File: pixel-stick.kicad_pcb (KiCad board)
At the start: 2 copper layers, 16.5 x 37.1 mm, 15 parts, among them J2 WS28**, U1 AZ1117-3.3, U2 ESP-01v090, U3 SN74LVC1T45DBV, U4 RT9361A

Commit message: address DRC errors
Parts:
- moved R3 5.94 mm to (55.5, 65.0)
- moved NT1 2.17 mm to (52.8, 83.6)
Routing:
- net Net-(R3-Pad1): track 4.21 -> 7.34 mm
- net +3V3: track 19.9 -> 16.9 mm
- net /GPIO0: track 27.3 -> 25.4 mm
- net /CLOCK: track 1.53 -> 3.17 mm
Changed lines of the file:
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@@
   )
   (setup
-    (last_trace_width 0.5)
+    (last_trace_width 0.25)
     (user_trace_width 0.5)
     (user_trace_width 1)
@@
   )
   (module NetTie:NetTie-2_SMD_Pad0.5mm (layer B.Cu)
-    (at 52.832 85.725 270)
+    (at 52.832 83.558 270)
     (descr "Net tie, 2 pin, 0.5mm square SMD pads")
     (tags "net tie")
@@
   )
   (module Resistor_SMD:R_0805_2012Metric (layer F.Cu)
-    (at 49.7055 66.548)
+    (at 55.4505 65.024)
     (descr "Resistor SMD 0805 (2012 Metric), square (rectangular) end terminal, IPC_7351 nominal, (Body size source: https://docs.google.com/spreadsheets/d/1BsfQQcO9C6DZCsRaXUlFlo91Tg2WpOkGARC1WS5S8t0/edit?usp=sharing), generated with kicad-footprint-generator")
     (tags resistor)
@@
   (segment (start 46.299999 70.393999) (end 48.668999 70.393999) (width 0.5) (layer F.Cu) (net 2))
   (segment (start 46.035 71.374) (end 46.035 70.658998) (width 0.5) (layer F.Cu) (net 2))
-  (segment (start 50.643 66.548) (end 50.643 67.348) (width 0.5) (layer F.Cu) (net 2))
-  (segment (start 50.643 64.775) (end 50.968 64.45) (width 0.5) (layer F.Cu) (net 2))
-  (segment (start 50.643 66.548) (end 50.643 64.775) (width 0.5) (layer F.Cu) (net 2))
   (segment (start 52.324 54.864) (end 55.946202 54.864) (width 1) (layer F.Cu) (net 2))
   (segment (start 52.04 56.485) (end 52.07 56.515) (width 0.25) (layer B.Cu) (net 2))
@@
   (segment (start 56.525836 87.132837) (end 56.510734 87.158438) (width 1) (layer F.Cu) (net 8))
   (segment (start 56.515 87.122) (end 56.525836 87.132837) (width 1) (layer F.Cu) (net 8))
-  (segment (start 52.832 87.249) (end 52.832 85.717) (width 1) (layer B.Cu) (net 10))
+  (segment (start 52.832 87.249) (end 52.832 84.074) (width 0.5) (layer B.Cu) (net 10))
   (segment (start 47.498 62.55) (end 48.768 62.55) (width 0.5) (layer F.Cu) (net 11))
   (via (at 47.498 62.55) (size 0.8) (drill 0.4) (layers F.Cu B.Cu) (net 11))
-  (segment (start 50.271679 65.323679) (end 47.897999 62.949999) (width 1) (layer B.Cu) (net 11))
-  (segment (start 50.271679 86.507321) (end 50.271679 65.323679) (width 1) (layer B.Cu) (net 11))
+  (segment (start 50.271679 65.323679) (end 47.897999 62.949999) (width 0.5) (layer B.Cu) (net 11))
+  (segment (start 50.271679 86.507321) (end 50.271679 65.323679) (width 0.5) (layer B.Cu) (net 11))
   (segment (start 47.897999 62.949999) (end 47.498 62.55) (width 1) (layer B.Cu) (net 11))
-  (segment (start 49.022 87.249) (end 50.271679 85.999321) (width 1) (layer B.Cu) (net 11))
-  (segment (start 52.832 63.578314) (end 52.832 85.02499) (width 1) (layer B.Cu) (net 12))
-  (segment (start 49.53 60.276314) (end 52.832 63.578314) (width 1) (layer B.Cu) (net 12))
-  (segment (start 49.53 59.055) (end 49.53 60.276314) (width 1) (layer B.Cu) (net 12))
+  (segment (start 49.022 87.249) (end 50.271679 85.999321) (width 0.5) (layer B.Cu) (net 11))
+  (segment (start 52.832 63.578314) (end 52.832 83.058) (width 0.5) (layer B.Cu) (net 12))
+  (segment (start 49.53 60.276314) (end 52.832 63.578314) (width 0.5) (layer B.Cu) (net 12))
+  (segment (start 49.53 59.055) (end 49.53 60.276314) (width 0.5) (layer B.Cu) (net 12))
   (segment (start 51.173 62.55) (end 50.968 62.55) (width 0.25) (layer F.Cu) (net 14))
   (segment (start 52.07 61.653) (end 51.173 62.55) (width 0.25) (layer F.Cu) (net 14))
   (segment (start 52.07 59.055) (end 52.07 61.653) (width 0.25) (layer F.Cu) (net 14))
-  (segment (start 49.623001 65.692999) (end 49.324237 65.991763) (width 0.25) (layer F.Cu) (net 15))
-  (segment (start 49.623001 63.575001) (end 49.623001 65.692999) (width 0.25) (layer F.Cu) (net 15))
   (segment (start 49.548 63.5) (end 49.623001 63.575001) (width 0.25) (layer F.Cu) (net 15))
-  (segment (start 49.324237 65.991763) (end 48.768 66.548) (width 0.25) (layer F.Cu) (net 15))
   (segment (start 48.768 63.5) (end 49.548 63.5) (width 0.25) (layer F.Cu) (net 15))
+  (segment (start 49.784 64.77) (end 50.340237 65.326237) (width 0.25) (layer F.Cu) (net 15))
+  (segment (start 49.784 63.736) (end 49.784 64.77) (width 0.25) (layer F.Cu) (net 15))
+  (segment (start 49.548 63.5) (end 49.784 63.736) (width 0.25) (layer F.Cu) (net 15))
+  (segment (start 53.9255 65.024) (end 54.513 65.024) (width 0.25) (layer F.Cu) (net 15))
+  (segment (start 53.623263 65.326237) (end 53.9255 65.024) (width 0.25) (layer F.Cu) (net 15))
+  (segment (start 50.340237 65.326237) (end 53.623263 65.326237) (width 0.25) (layer F.Cu) (net 15))
   (zone (net 1) (net_name GND) (layer F.Cu) (hatch edge 0.508)
     (connect_pads (clearance 0.508))
@@
     (polygon
       (pts
-        (xy 42.672 57.912) (xy 48.312438 57.912) (xy 48.26 73.66) (xy 53.25 73.66) (xy 53.25 76.25)
-        (xy 55.75 76.25) (xy 55.75 78.74) (xy 49.276 78.74) (xy 49.276 82.804) (xy 53.975 82.804)
+        (xy 42.672 57.912) (xy 48.006 57.912) (xy 48.006 73.66) (xy 53.25 73.66) (xy 53.25 76.25)
+        (xy 55.626 76.25) (xy 55.626 78.486) (xy 49.022 78.486) (xy 49.022 83.058) (xy 53.975 83.058)
         (xy 53.975 90.17) (xy 42.672 90.424)
       )
@@
     (polygon
       (pts
-        (xy 56 73.66) (xy 59 73.66) (xy 58.875 82.55) (xy 49.53 82.55) (xy 49.53 79)
-        (xy 56 79)
+        (xy 56.134 73.66) (xy 59 73.66) (xy 58.875 82.55) (xy 49.53 82.55) (xy 49.53 79)
+        (xy 56.134 78.994)
       )
     )

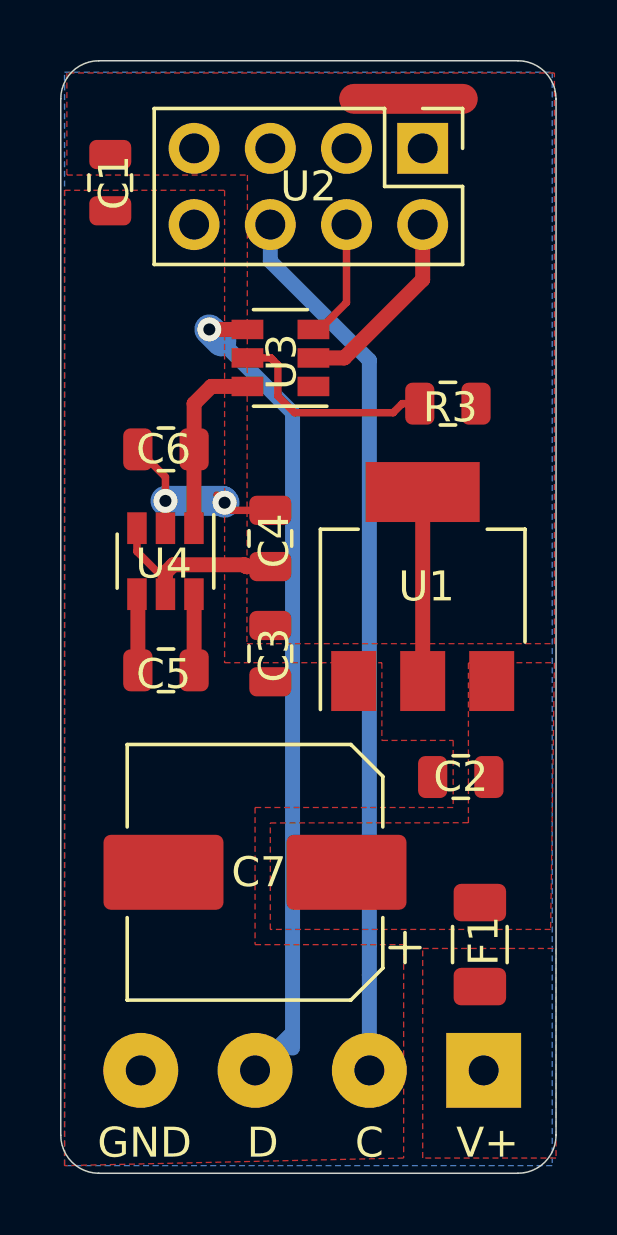
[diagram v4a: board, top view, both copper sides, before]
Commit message: consilidate parts on pcb
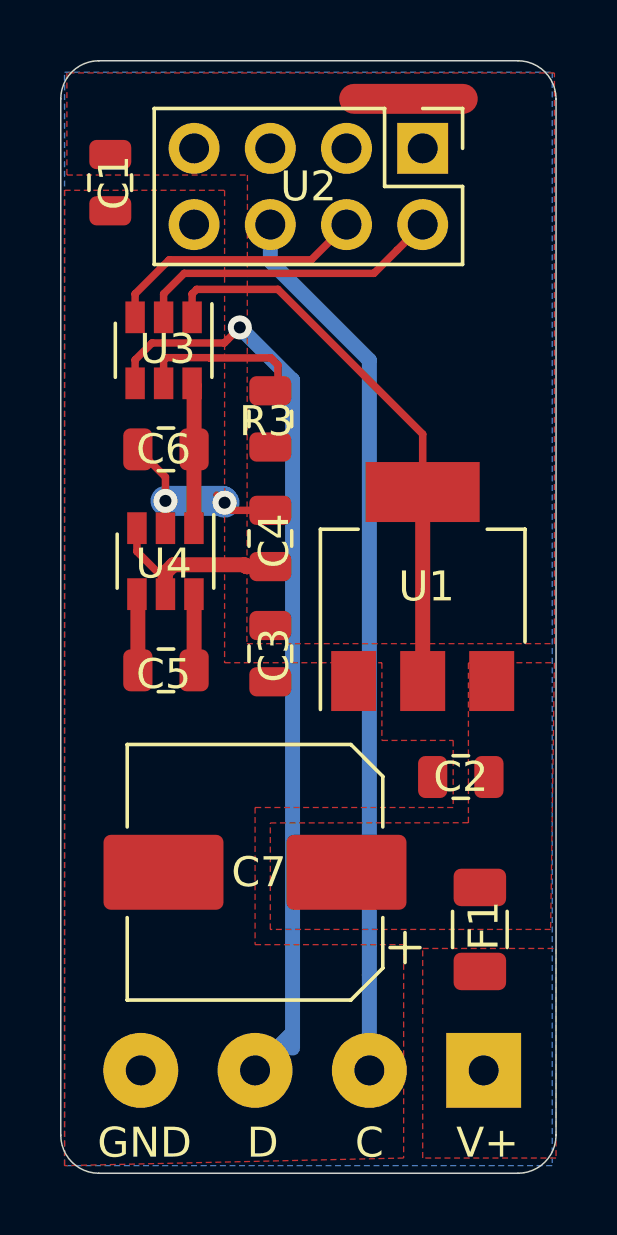
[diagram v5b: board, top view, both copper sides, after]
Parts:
- moved R3 5.94 mm to (49.5, 65.5), turned to 270 degrees
- moved U3 3.90 mm to (46.0, 63.2), turned to 270 degrees
- moved F1 0.51 mm to (56.5, 82.5)
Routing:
- net +3V3: track 16.9 -> 29.4 mm
- net /GPIO2: track 4.07 -> 8.78 mm
- net GND: track 13.5 -> 17.4 mm
- net /DATA: track 28.1 -> 31.2 mm
- net Net-(R3-Pad1): track 7.34 -> 5.86 mm
- net +5V: track 6.17 -> 4.86 mm

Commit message: more layer cleanup
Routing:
- net GND: track 17.4 -> 14.9 mm, vias 2 -> 1
- net /DATA: track 31.2 -> 29.7 mm
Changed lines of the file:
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@@
     (thickness 1.6)
     (drawings 13)
-    (tracks 66)
+    (tracks 61)
     (zones 0)
     (modules 15)
@@
   )
   (setup
-    (last_trace_width 0.25)
+    (last_trace_width 0.5)
     (user_trace_width 0.5)
     (user_trace_width 1)
@@
   (gr_line (start 43.815 90.678) (end 57.785 90.678) (layer Edge.Cuts) (width 0.05))
   (gr_line (start 42.545 54.864) (end 42.545 89.408) (layer Edge.Cuts) (width 0.05))
-  (segment (start 46.035 67.468) (end 46.035 68.265) (width 0.25) (layer F.Cu) (net 1))
-  (segment (start 45.115 66.548) (end 46.035 67.468) (width 0.25) (layer F.Cu) (net 1))
-  (segment (start 49.53 68.58) (end 48.26 68.58) (width 0.25) (layer F.Cu) (net 1))
-  (segment (start 48.26 68.58) (end 48.006 68.326) (width 0.25) (layer F.Cu) (net 1))
-  (segment (start 48.006 68.326) (end 47.752 68.072) (width 0.25) (layer F.Cu) (net 1))
-  (via (at 48.006 68.326) (size 0.8) (drill 0.4) (layers F.Cu B.Cu) (net 1) (status 1000000))
+  (via (at 48.006 68.326) (size 0.8) (drill 0.4) (layers F.Cu B.Cu) (net 1))
   (segment (start 46.035 68.265) (end 46.035 69.174) (width 0.25) (layer F.Cu) (net 1))
-  (via (at 46.035 68.265) (size 0.8) (drill 0.4) (layers F.Cu B.Cu) (net 1))
   (segment (start 47.945 68.265) (end 48.006 68.326) (width 1) (layer B.Cu) (net 1))
   (segment (start 46.035 68.265) (end 47.945 68.265) (width 1) (layer B.Cu) (net 1))
@@
   (segment (start 52.984989 60.680011) (end 53.760001 59.904999) (width 0.25) (layer F.Cu) (net 1))
   (segment (start 45.974 62.146) (end 45.974 61.366) (width 0.25) (layer F.Cu) (net 1))
+  (segment (start 48.26 68.58) (end 48.006 68.326) (width 0.5) (layer F.Cu) (net 1))
+  (segment (start 49.53 68.58) (end 48.26 68.58) (width 0.5) (layer F.Cu) (net 1))
   (segment (start 45.085 69.954) (end 46.035 70.904) (width 0.25) (layer F.Cu) (net 2))
   (segment (start 46.035 70.904) (end 46.035 71.374) (width 0.25) (layer F.Cu) (net 2))
@@
   (segment (start 52.832 87.249) (end 52.832 84.074) (width 0.5) (layer B.Cu) (net 10))
   (via (at 48.514 62.484) (size 0.8) (drill 0.4) (layers F.Cu B.Cu) (net 11))
-  (segment (start 49.022 87.249) (end 50.271679 85.999321) (width 0.5) (layer B.Cu) (net 11))
   (segment (start 48.114001 62.883999) (end 48.514 62.484) (width 0.25) (layer F.Cu) (net 11))
   (segment (start 47.996999 63.001001) (end 48.114001 62.883999) (width 0.25) (layer F.Cu) (net 11))
@@
   (segment (start 45.024 63.566) (end 45.588999 63.001001) (width 0.25) (layer F.Cu) (net 11))
   (segment (start 45.024 64.346) (end 45.024 63.566) (width 0.25) (layer F.Cu) (net 11))
-  (segment (start 50.271679 64.241679) (end 48.514 62.484) (width 0.5) (layer B.Cu) (net 11))
-  (segment (start 50.271679 86.507321) (end 50.271679 64.241679) (width 0.5) (layer B.Cu) (net 11))
+  (segment (start 49.022 62.992) (end 48.514 62.484) (width 0.5) (layer B.Cu) (net 11))
+  (segment (start 49.022 87.249) (end 49.022 62.992) (width 0.5) (layer B.Cu) (net 11))
   (segment (start 52.832 63.578314) (end 52.832 83.058) (width 0.5) (layer B.Cu) (net 12))
   (segment (start 49.53 60.276314) (end 52.832 63.578314) (width 0.5) (layer B.Cu) (net 12))
@@
     (polygon
       (pts
-        (xy 42.672 57.912) (xy 48.006 57.912) (xy 48.006 73.66) (xy 53.25 73.66) (xy 53.25 76.25)
+        (xy 42.672 57.912) (xy 47.752 57.912) (xy 47.752 73.66) (xy 53.25 73.66) (xy 53.25 76.25)
         (xy 55.626 76.25) (xy 55.626 78.486) (xy 49.022 78.486) (xy 49.022 83.058) (xy 53.975 83.058)
         (xy 53.975 90.17) (xy 42.672 90.424)

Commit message: more power/gnd plane cleanup
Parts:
- moved J2 0.25 mm to (56.4, 87.2)
- turned C4 to 270 degrees
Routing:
- net GND: track 14.9 -> 18.3 mm, vias 1 -> 0
- net +3V3: track 29.4 -> 26.5 mm
